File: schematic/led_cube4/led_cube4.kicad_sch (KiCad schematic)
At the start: 13 parts, among them SW1 SW_Push, U1 L7805, U2 ATmega16A-P, Y1 14.7456MHz

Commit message: feat(schematic): add programming connector
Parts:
- added J2: Conn_01x08_Pin, symbol Connector:Conn_01x08_Pin
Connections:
- net +5V: now also J2.2 (Pin_2)
- net GND: now also J2.3 (Pin_3)
- net MOSI: now reaches U2.6 (PB5)
- net MOSI: now also J2.7 (Pin_7)
- net MISO: now reaches U2.7 (PB6)
- net MISO: now also J2.4 (Pin_4)
- net SCK: now reaches U2.8 (PB7)
- net SCK: now also J2.5 (Pin_5)
- net RESET: now reaches SW1.2, U2.9 (~{RESET})
- net RESET: now also J2.6 (Pin_6)
- no-connect marks 0 -> 2
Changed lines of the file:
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@@
   (junction (at 80.01 68.58) (diameter 0) (color 0 0 0 0)
   )
+  (junction (at 60.96 83.82) (diameter 0) (color 0 0 0 0)
+  )
   (junction (at 53.34 88.9) (diameter 0) (color 0 0 0 0)
   )
@@
   (junction (at 100.33 30.48) (diameter 0) (color 0 0 0 0)
   )
+  (no_connect (at 39.37 176.53))
+  (no_connect (at 39.37 158.75))
   (wire (pts (xy 77.47 59.69) (xy 81.28 59.69))
     (stroke (width 0) (type default))
@@
     (stroke (width 0) (type default))
   )
+  (wire (pts (xy 40.64 166.37) (xy 39.37 166.37))
+    (stroke (width 0) (type default))
+  )
+  (wire (pts (xy 92.71 124.46) (xy 93.98 124.46))
+    (stroke (width 0) (type default))
+  )
   (wire (pts (xy 50.8 76.2) (xy 60.96 76.2))
     (stroke (width 0) (type default))
   )
+  (wire (pts (xy 39.37 171.45) (xy 40.64 171.45))
+    (stroke (width 0) (type default))
+  )
   (wire (pts (xy 88.9 68.58) (xy 92.71 68.58))
     (stroke (width 0) (type default))
@@
     (stroke (width 0) (type default))
   )
+  (wire (pts (xy 93.98 121.92) (xy 92.71 121.92))
+    (stroke (width 0) (type default))
+  )
   (wire (pts (xy 35.56 99.06) (xy 35.56 101.6))
     (stroke (width 0) (type default))
   )
+  (wire (pts (xy 39.37 168.91) (xy 40.64 168.91))
+    (stroke (width 0) (type default))
+  )
   (wire (pts (xy 92.71 68.58) (xy 92.71 71.12))
     (stroke (width 0) (type default))
@@
     (stroke (width 0) (type default))
   )
+  (wire (pts (xy 39.37 173.99) (xy 40.64 173.99))
+    (stroke (width 0) (type default))
+  )
+  (wire (pts (xy 39.37 163.83) (xy 50.8 163.83))
+    (stroke (width 0) (type default))
+  )
+  (wire (pts (xy 59.69 83.82) (xy 60.96 83.82))
+    (stroke (width 0) (type default))
+  )
   (wire (pts (xy 60.96 76.2) (xy 60.96 83.82))
     (stroke (width 0) (type default))
@@
     (stroke (width 0) (type default))
   )
+  (wire (pts (xy 50.8 163.83) (xy 50.8 179.07))
+    (stroke (width 0) (type default))
+  )
   (wire (pts (xy 100.33 30.48) (xy 100.33 31.75))
     (stroke (width 0) (type default))
@@
     (stroke (width 0) (type default))
   )
+  (wire (pts (xy 92.71 119.38) (xy 93.98 119.38))
+    (stroke (width 0) (type default))
+  )
   (wire (pts (xy 36.83 33.02) (xy 35.56 33.02))
     (stroke (width 0) (type default))
   )
+  (wire (pts (xy 50.8 161.29) (xy 50.8 157.48))
+    (stroke (width 0) (type default))
+  )
   (wire (pts (xy 57.15 30.48) (xy 57.15 31.75))
     (stroke (width 0) (type default))
   )
+  (wire (pts (xy 39.37 161.29) (xy 50.8 161.29))
+    (stroke (width 0) (type default))
+  )
   (wire (pts (xy 100.33 29.21) (xy 100.33 30.48))
     (stroke (width 0) (type default))
@@
   (wire (pts (xy 35.56 76.2) (xy 35.56 78.74))
     (stroke (width 0) (type default))
+  )
+  (global_label "SCK" (shape output) (at 93.98 124.46 0) (fields_autoplaced)
+    (effects (font (size 1.27 1.27)) (justify left))
+    (property "Intersheetrefs" "${INTERSHEET_REFS}" (at 100.7147 124.46 0)
+      (effects (font (size 1.27 1.27)) (justify left) hide)
+    )
+  )
+  (global_label "MOSI" (shape output) (at 93.98 119.38 0) (fields_autoplaced)
+    (effects (font (size 1.27 1.27)) (justify left))
+    (property "Intersheetrefs" "${INTERSHEET_REFS}" (at 101.5614 119.38 0)
+      (effects (font (size 1.27 1.27)) (justify left) hide)
+    )
+  )
+  (global_label "SCK" (shape input) (at 40.64 168.91 0) (fields_autoplaced)
+    (effects (font (size 1.27 1.27)) (justify left))
+    (property "Intersheetrefs" "${INTERSHEET_REFS}" (at 47.3747 168.91 0)
+      (effects (font (size 1.27 1.27)) (justify left) hide)
+    )
+  )
+  (global_label "MISO" (shape input) (at 93.98 121.92 0) (fields_autoplaced)
+    (effects (font (size 1.27 1.27)) (justify left))
+    (property "Intersheetrefs" "${INTERSHEET_REFS}" (at 101.5614 121.92 0)
+      (effects (font (size 1.27 1.27)) (justify left) hide)
+    )
+  )
+  (global_label "RESET" (shape input) (at 59.69 83.82 180) (fields_autoplaced)
+    (effects (font (size 1.27 1.27)) (justify right))
+    (property "Intersheetrefs" "${INTERSHEET_REFS}" (at 50.9597 83.82 0)
+      (effects (font (size 1.27 1.27)) (justify right) hide)
+    )
+  )
+  (global_label "RESET" (shape output) (at 40.64 171.45 0) (fields_autoplaced)
+    (effects (font (size 1.27 1.27)) (justify left))
+    (property "Intersheetrefs" "${INTERSHEET_REFS}" (at 49.3703 171.45 0)
+      (effects (font (size 1.27 1.27)) (justify left) hide)
+    )
+  )
+  (global_label "MISO" (shape output) (at 40.64 166.37 0) (fields_autoplaced)
+    (effects (font (size 1.27 1.27)) (justify left))
+    (property "Intersheetrefs" "${INTERSHEET_REFS}" (at 48.2214 166.37 0)
+      (effects (font (size 1.27 1.27)) (justify left) hide)
+    )
+  )
+  (global_label "MOSI" (shape input) (at 40.64 173.99 0) (fields_autoplaced)
+    (effects (font (size 1.27 1.27)) (justify left))
+    (property "Intersheetrefs" "${INTERSHEET_REFS}" (at 48.2214 173.99 0)
+      (effects (font (size 1.27 1.27)) (justify left) hide)
+    )
   )
   (symbol (lib_id "power:GND") (at 87.63 40.64 0) (unit 1)
@@
     )
   )
+  (symbol (lib_id "power:GND") (at 50.8 179.07 0) (unit 1)
+    (in_bom yes) (on_board yes) (dnp no) (fields_autoplaced)
+    (property "Reference" "#PWR015" (at 50.8 185.42 0)
+      (effects (font (size 1.27 1.27)) hide)
+    )
+    (property "Value" "GND" (at 50.8 184.15 0)
+      (effects (font (size 1.27 1.27)))
+    )
+    (property "Footprint" "" (at 50.8 179.07 0)
+      (effects (font (size 1.27 1.27)) hide)
+    )
+    (property "Datasheet" "" (at 50.8 179.07 0)
+      (effects (font (size 1.27 1.27)) hide)
+    )
+    (pin "1")
+    (instances
+      (project "led_cube4"
+        (path "/44967cb4-81e9-43f0-83d3-71e4b89b9f9f"
+          (reference "#PWR015") (unit 1)
+        )
+      )
+    )
+  )
   (symbol (lib_id "power:GND") (at 35.56 78.74 0) (unit 1)
     (in_bom yes) (on_board yes) (dnp no) (fields_autoplaced)
@@
     )
   )
+  (symbol (lib_id "power:+5V") (at 50.8 157.48 0) (unit 1)
+    (in_bom yes) (on_board yes) (dnp no) (fields_autoplaced)
+    (property "Reference" "#PWR014" (at 50.8 161.29 0)
+      (effects (font (size 1.27 1.27)) hide)
+    )
+    (property "Value" "+5V" (at 50.8 152.4 0)
+      (effects (font (size 1.27 1.27)))
+    )
+    (property "Footprint" "" (at 50.8 157.48 0)
+      (effects (font (size 1.27 1.27)) hide)
+    )
+    (property "Datasheet" "" (at 50.8 157.48 0)
+      (effects (font (size 1.27 1.27)) hide)
+    )
+    (pin "1")
+    (instances
+      (project "led_cube4"
+        (path "/44967cb4-81e9-43f0-83d3-71e4b89b9f9f"
+          (reference "#PWR014") (unit 1)
+        )
+      )
+    )
+  )
   (symbol (lib_id "power:GND") (at 36.83 40.64 0) (unit 1)
     (in_bom yes) (on_board yes) (dnp no) (fields_autoplaced)
@@
         )
       )
+    )
+  )
+  (symbol (lib_id "Connector:Conn_01x08_Pin") (at 34.29 166.37 0) (unit 1)
+    (in_bom yes) (on_board yes) (dnp no)
+    (property "Reference" "J2" (at 34.925 153.67 0)
+      (effects (font (size 1.27 1.27)))
+    )
+    (property "Value" "Conn_01x08_Pin" (at 34.925 156.21 0)
+      (effects (font (size 1.27 1.27)) hide)
+    )
+    (property "Footprint" "" (at 34.29 166.37 0)
+      (effects (font (size 1.27 1.27)) hide)
+    )
+    (property "Datasheet" "~" (at 34.29 166.37 0)
+      (effects (font (size 1.27 1.27)) hide)
+    )
+    (pin "4")
+    (pin "6")
+    (pin "2")
+    (pin "5")
+    (pin "7")
+    (pin "3")
+    (pin "1")
+    (pin "8")
+    (instances
+      (project "led_cube4"
+        (path "/44967cb4-81e9-43f0-83d3-71e4b89b9f9f"
+          (reference "J2") (unit 1)
+        )
+      )

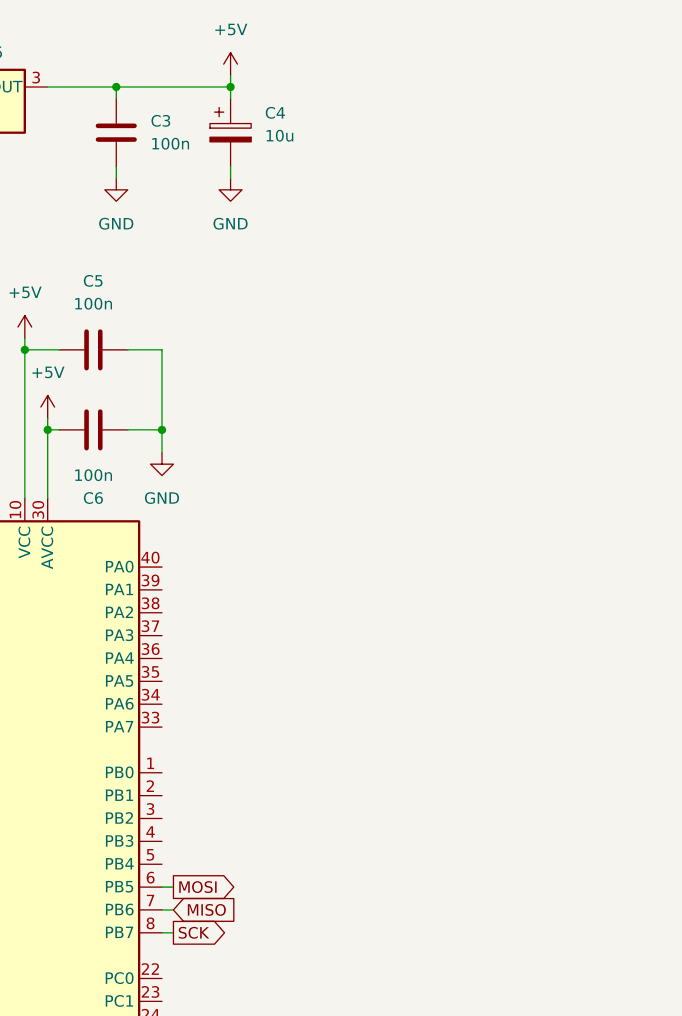
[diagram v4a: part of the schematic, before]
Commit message: feat(schematic): add functional buttons
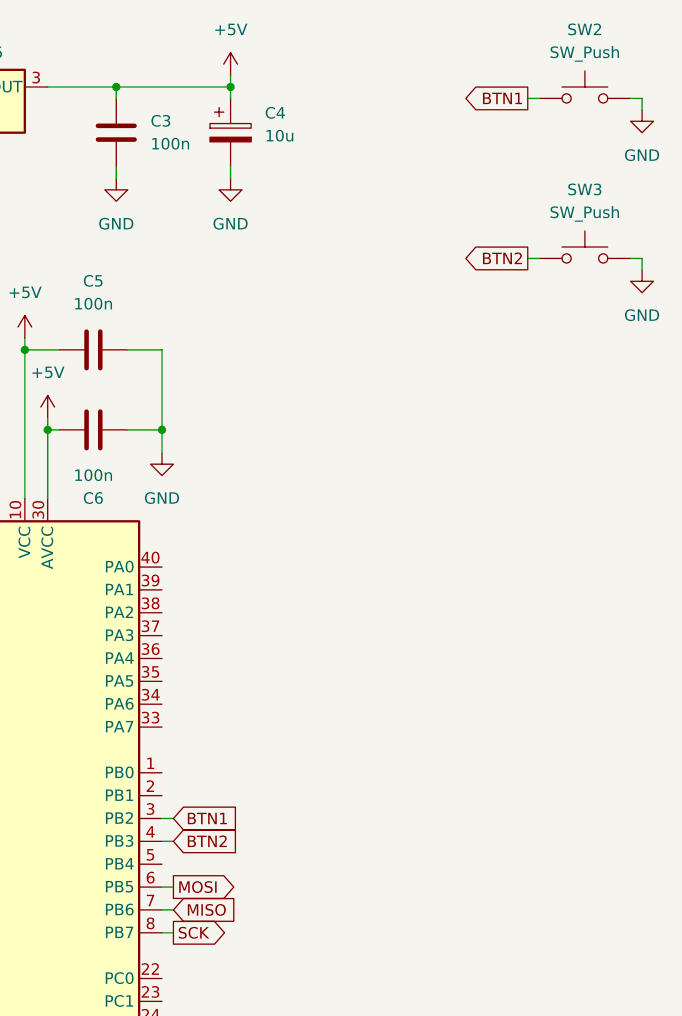
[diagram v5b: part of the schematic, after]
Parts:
- added SW2, SW3: SW_Push, symbol Switch:SW_Push
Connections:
- net GND: now also SW2.2, SW3.2
- net BTN1: now reaches U2.3 (PB2)
- net BTN1: now also SW2.1
- net BTN2: now reaches U2.4 (PB3)
- net BTN2: now also SW3.1
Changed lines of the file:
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@@
+    (stroke (width 0) (type default))
+  )
+  (wire (pts (xy 92.71 114.3) (xy 93.98 114.3))
     (stroke (width 0) (type default))
   )
@@
     (stroke (width 0) (type default))
   )
+  (wire (pts (xy 133.35 31.75) (xy 134.62 31.75))
+    (stroke (width 0) (type default))
+  )
   (wire (pts (xy 44.45 30.48) (xy 57.15 30.48))
     (stroke (width 0) (type default))
@@
     (stroke (width 0) (type default))
   )
+  (wire (pts (xy 92.71 111.76) (xy 93.98 111.76))
+    (stroke (width 0) (type default))
+  )
   (wire (pts (xy 87.63 30.48) (xy 87.63 31.75))
     (stroke (width 0) (type default))
@@
     (stroke (width 0) (type default))
   )
+  (wire (pts (xy 144.78 31.75) (xy 146.05 31.75))
+    (stroke (width 0) (type default))
+  )
+  (wire (pts (xy 133.35 49.53) (xy 134.62 49.53))
+    (stroke (width 0) (type default))
+  )
   (wire (pts (xy 77.47 59.69) (xy 77.47 76.2))
     (stroke (width 0) (type default))
@@
     (stroke (width 0) (type default))
   )
+  (wire (pts (xy 146.05 49.53) (xy 146.05 50.8))
+    (stroke (width 0) (type default))
+  )
   (wire (pts (xy 53.34 97.79) (xy 53.34 99.06))
     (stroke (width 0) (type default))
   )
+  (wire (pts (xy 146.05 31.75) (xy 146.05 33.02))
+    (stroke (width 0) (type default))
+  )
   (wire (pts (xy 100.33 39.37) (xy 100.33 40.64))
     (stroke (width 0) (type default))
@@
     (stroke (width 0) (type default))
   )
+  (wire (pts (xy 144.78 49.53) (xy 146.05 49.53))
+    (stroke (width 0) (type default))
+  )
   (wire (pts (xy 36.83 40.64) (xy 36.83 33.02))
     (stroke (width 0) (type default))
@@
     )
   )
+  (global_label "BTN1" (shape output) (at 133.35 31.75 180) (fields_autoplaced)
+    (effects (font (size 1.27 1.27)) (justify right))
+    (property "Intersheetrefs" "${INTERSHEET_REFS}" (at 125.5872 31.75 0)
+      (effects (font (size 1.27 1.27)) (justify right) hide)
+    )
+  )
+  (global_label "BTN1" (shape input) (at 93.98 111.76 0) (fields_autoplaced)
+    (effects (font (size 1.27 1.27)) (justify left))
+    (property "Intersheetrefs" "${INTERSHEET_REFS}" (at 101.7428 111.76 0)
+      (effects (font (size 1.27 1.27)) (justify left) hide)
+    )
+  )
   (global_label "MOSI" (shape output) (at 93.98 119.38 0) (fields_autoplaced)
     (effects (font (size 1.27 1.27)) (justify left))
@@
     (property "Intersheetrefs" "${INTERSHEET_REFS}" (at 101.5614 121.92 0)
       (effects (font (size 1.27 1.27)) (justify left) hide)
+    )
+  )
+  (global_label "BTN2" (shape output) (at 133.35 49.53 180) (fields_autoplaced)
+    (effects (font (size 1.27 1.27)) (justify right))
+    (property "Intersheetrefs" "${INTERSHEET_REFS}" (at 125.5872 49.53 0)
+      (effects (font (size 1.27 1.27)) (justify right) hide)
     )
   )
@@
     )
   )
+  (global_label "BTN2" (shape input) (at 93.98 114.3 0) (fields_autoplaced)
+    (effects (font (size 1.27 1.27)) (justify left))
+    (property "Intersheetrefs" "${INTERSHEET_REFS}" (at 101.7428 114.3 0)
+      (effects (font (size 1.27 1.27)) (justify left) hide)
+    )
+  )
   (global_label "MOSI" (shape input) (at 40.64 173.99 0) (fields_autoplaced)
     (effects (font (size 1.27 1.27)) (justify left))
@@
     )
   )
+  (symbol (lib_id "power:GND") (at 146.05 50.8 0) (unit 1)
+    (in_bom yes) (on_board yes) (dnp no) (fields_autoplaced)
+    (property "Reference" "#PWR016" (at 146.05 57.15 0)
+      (effects (font (size 1.27 1.27)) hide)
+    )
+    (property "Value" "GND" (at 146.05 55.88 0)
+      (effects (font (size 1.27 1.27)))
+    )
+    (property "Footprint" "" (at 146.05 50.8 0)
+      (effects (font (size 1.27 1.27)) hide)
+    )
+    (property "Datasheet" "" (at 146.05 50.8 0)
+      (effects (font (size 1.27 1.27)) hide)
+    )
+    (pin "1")
+    (instances
+      (project "led_cube4"
+        (path "/44967cb4-81e9-43f0-83d3-71e4b89b9f9f"
+          (reference "#PWR016") (unit 1)
+        )
+      )
+    )
+  )
   (symbol (lib_id "power:GND") (at 57.15 40.64 0) (unit 1)
     (in_bom yes) (on_board yes) (dnp no) (fields_autoplaced)
@@
         (path "/44967cb4-81e9-43f0-83d3-71e4b89b9f9f"
           (reference "#PWR010") (unit 1)
+        )
+      )
+    )
+  )
+  (symbol (lib_id "Switch:SW_Push") (at 139.7 49.53 0) (unit 1)
+    (in_bom yes) (on_board yes) (dnp no) (fields_autoplaced)
+    (property "Reference" "SW3" (at 139.7 41.91 0)
+      (effects (font (size 1.27 1.27)))
+    )
+    (property "Value" "SW_Push" (at 139.7 44.45 0)
+      (effects (font (size 1.27 1.27)))
+    )
+    (property "Footprint" "" (at 139.7 44.45 0)
+      (effects (font (size 1.27 1.27)) hide)
+    )
+    (property "Datasheet" "~" (at 139.7 44.45 0)
+      (effects (font (size 1.27 1.27)) hide)
+    )
+    (pin "2")
+    (pin "1")
+    (instances
+      (project "led_cube4"
+        (path "/44967cb4-81e9-43f0-83d3-71e4b89b9f9f"
+          (reference "SW3") (unit 1)
         )
       )
@@
     )
   )
+  (symbol (lib_id "power:GND") (at 146.05 33.02 0) (unit 1)
+    (in_bom yes) (on_board yes) (dnp no) (fields_autoplaced)
+    (property "Reference" "#PWR017" (at 146.05 39.37 0)
+      (effects (font (size 1.27 1.27)) hide)
+    )
+    (property "Value" "GND" (at 146.05 38.1 0)
+      (effects (font (size 1.27 1.27)))
+    )
+    (property "Footprint" "" (at 146.05 33.02 0)
+      (effects (font (size 1.27 1.27)) hide)
+    )
+    (property "Datasheet" "" (at 146.05 33.02 0)
+      (effects (font (size 1.27 1.27)) hide)
+    )
+    (pin "1")
+    (instances
+      (project "led_cube4"
+        (path "/44967cb4-81e9-43f0-83d3-71e4b89b9f9f"
+          (reference "#PWR017") (unit 1)
+        )
+      )
+    )
+  )
   (symbol (lib_id "Device:C_Polarized") (at 44.45 35.56 0) (unit 1)
     (in_bom yes) (on_board yes) (dnp no) (fields_autoplaced)
@@
         )
       )
+    )
+  )
+  (symbol (lib_id "Switch:SW_Push") (at 139.7 31.75 0) (unit 1)
+    (in_bom yes) (on_board yes) (dnp no) (fields_autoplaced)
+    (property "Reference" "SW2" (at 139.7 24.13 0)
+      (effects (font (size 1.27 1.27)))
+    )
+    (property "Value" "SW_Push" (at 139.7 26.67 0)
+      (effects (font (size 1.27 1.27)))
+    )
+    (property "Footprint" "" (at 139.7 26.67 0)
+      (effects (font (size 1.27 1.27)) hide)
+    )
+    (property "Datasheet" "~" (at 139.7 26.67 0)
+      (effects (font (size 1.27 1.27)) hide)
+    )
+    (pin "2")
+    (pin "1")
+    (instances
+      (project "led_cube4"
+        (path "/44967cb4-81e9-43f0-83d3-71e4b89b9f9f"
+          (reference "SW2") (unit 1)
+        )
+      )

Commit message: fix(schematic): add 10k pull-up resistor to the reset circuit
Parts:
- added R1: 10k, symbol Device:R
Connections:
- net +5V: now also R1.1
- net RESET: now also R1.2
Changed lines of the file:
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@@
   (junction (at 35.56 99.06) (diameter 0) (color 0 0 0 0)
+  )
+  (junction (at 60.96 76.2) (diameter 0) (color 0 0 0 0)
   )
   (junction (at 80.01 68.58) (diameter 0) (color 0 0 0 0)
@@
     (stroke (width 0) (type default))
   )
+  (wire (pts (xy 60.96 74.93) (xy 60.96 76.2))
+    (stroke (width 0) (type default))
+  )
   (wire (pts (xy 133.35 49.53) (xy 134.62 49.53))
     (stroke (width 0) (type default))
@@
   )
   (wire (pts (xy 92.71 119.38) (xy 93.98 119.38))
+    (stroke (width 0) (type default))
+  )
+  (wire (pts (xy 60.96 66.04) (xy 60.96 67.31))
     (stroke (width 0) (type default))
   )
@@
     )
   )
+  (symbol (lib_id "power:+5V") (at 60.96 66.04 0) (unit 1)
+    (in_bom yes) (on_board yes) (dnp no) (fields_autoplaced)
+    (property "Reference" "#PWR018" (at 60.96 69.85 0)
+      (effects (font (size 1.27 1.27)) hide)
+    )
+    (property "Value" "+5V" (at 60.96 60.96 0)
+      (effects (font (size 1.27 1.27)))
+    )
+    (property "Footprint" "" (at 60.96 66.04 0)
+      (effects (font (size 1.27 1.27)) hide)
+    )
+    (property "Datasheet" "" (at 60.96 66.04 0)
+      (effects (font (size 1.27 1.27)) hide)
+    )
+    (pin "1")
+    (instances
+      (project "led_cube4"
+        (path "/44967cb4-81e9-43f0-83d3-71e4b89b9f9f"
+          (reference "#PWR018") (unit 1)
+        )
+      )
+    )
+  )
   (symbol (lib_id "power:+5V") (at 100.33 29.21 0) (unit 1)
     (in_bom yes) (on_board yes) (dnp no) (fields_autoplaced)
@@
         )
       )
+    )
+  )
+  (symbol (lib_id "Device:R") (at 60.96 71.12 0) (unit 1)
+    (in_bom yes) (on_board yes) (dnp no) (fields_autoplaced)
+    (property "Reference" "R1" (at 63.5 69.85 0)
+      (effects (font (size 1.27 1.27)) (justify left))
+    )
+    (property "Value" "10k" (at 63.5 72.39 0)
+      (effects (font (size 1.27 1.27)) (justify left))
+    )
+    (property "Footprint" "" (at 59.182 71.12 90)
+      (effects (font (size 1.27 1.27)) hide)
+    )
+    (property "Datasheet" "~" (at 60.96 71.12 0)
+      (effects (font (size 1.27 1.27)) hide)
+    )
+    (pin "1")
+    (pin "2")
+    (instances
+      (project "led_cube4"
+        (path "/44967cb4-81e9-43f0-83d3-71e4b89b9f9f"
+          (reference "R1") (unit 1)
+        )
+      )
